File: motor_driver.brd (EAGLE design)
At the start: 38.1 x 34.6 mm, 15 parts

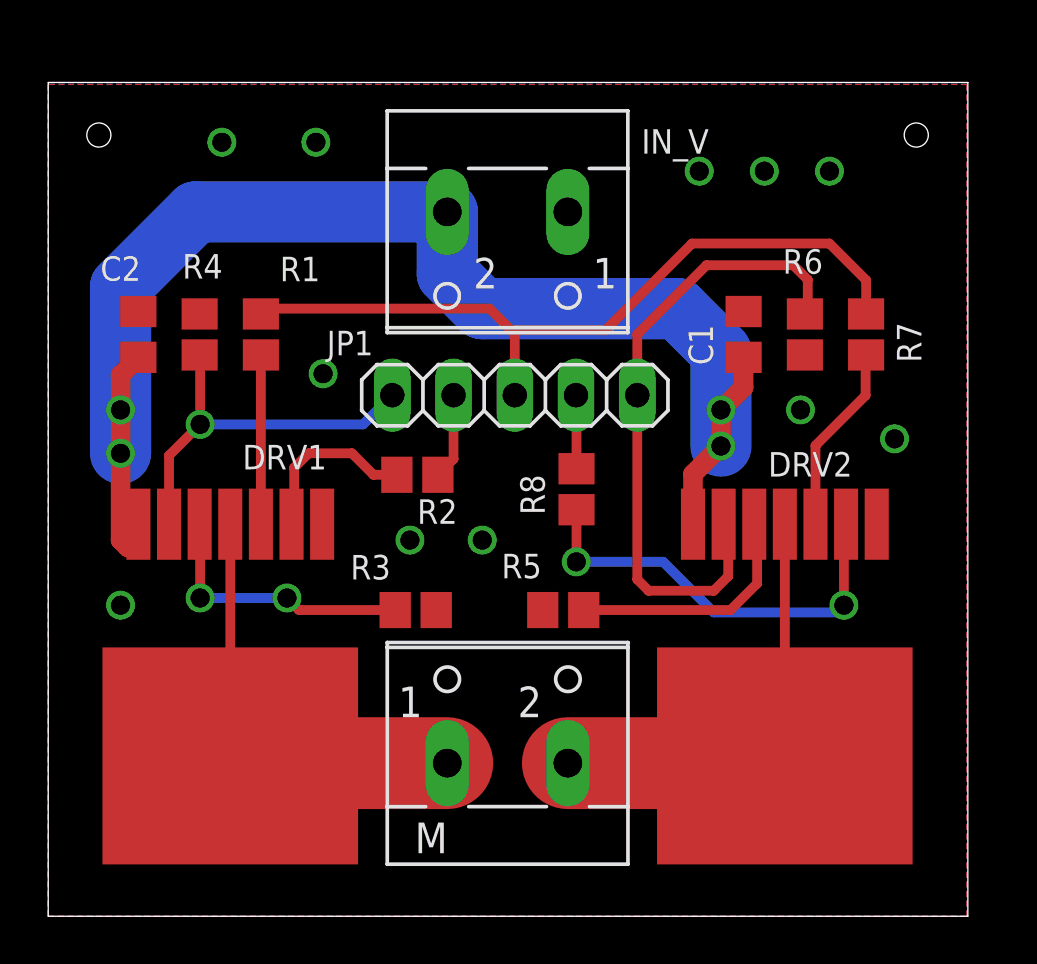
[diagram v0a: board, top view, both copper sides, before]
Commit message: Widened supply wires on the driver, changed wire positions on control panel board.
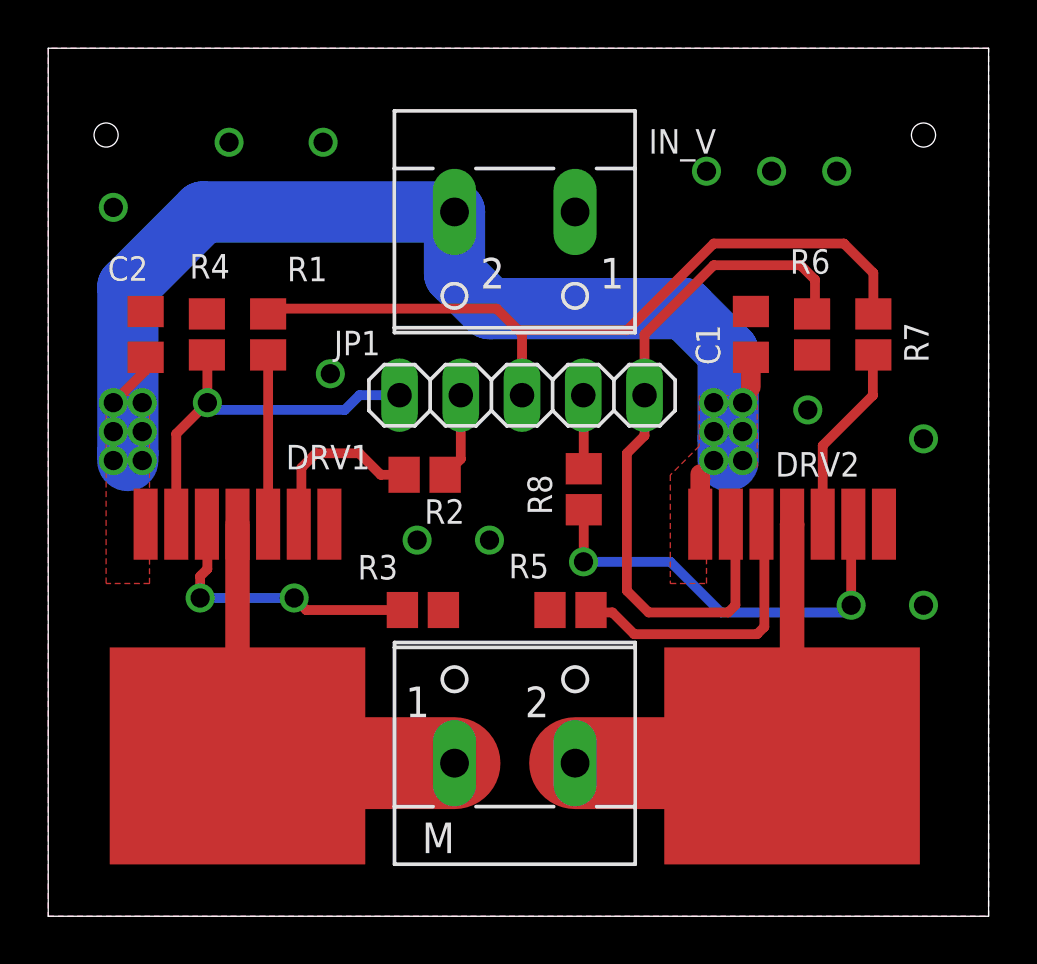
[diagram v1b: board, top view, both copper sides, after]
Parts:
- moved C1 0.30 mm to (29.1, 24.1)
- moved DRV2 0.30 mm to (30.9, 6.65)
- moved IN_V 0.30 mm to (19.4, 27.9)
- moved M 0.30 mm to (19.4, 7.62)
- moved R5 0.30 mm to (21.7, 12.7)
- moved R6 0.30 mm to (31.7, 24.1)
- moved R8 0.30 mm to (22.2, 17.7)
- moved C2 0.30 mm to (4.04, 24.1)
- moved DRV1 0.30 mm to (7.85, 6.65)
- moved R4 0.30 mm to (6.58, 24.1)
- moved R1 0.30 mm to (9.12, 24.1)
- moved R2 0.30 mm to (15.6, 18.3)
- moved R3 0.30 mm to (15.5, 12.7)
- moved JP1 0.30 mm to (19.6, 21.6)
- moved R7 0.30 mm to (34.2, 24.1)
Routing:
- net VSS: track 58.1 -> 49.8 mm, vias 4 -> 12
- net N$10: track 26.6 -> 29.3 mm
- net N$8: track 10.2 -> 12.0 mm
- added copper zone on layer 1, net VSS
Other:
- board size 38.1 x 34.6 mm -> 39 x 36 mm
